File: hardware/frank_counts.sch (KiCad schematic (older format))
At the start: 1 part

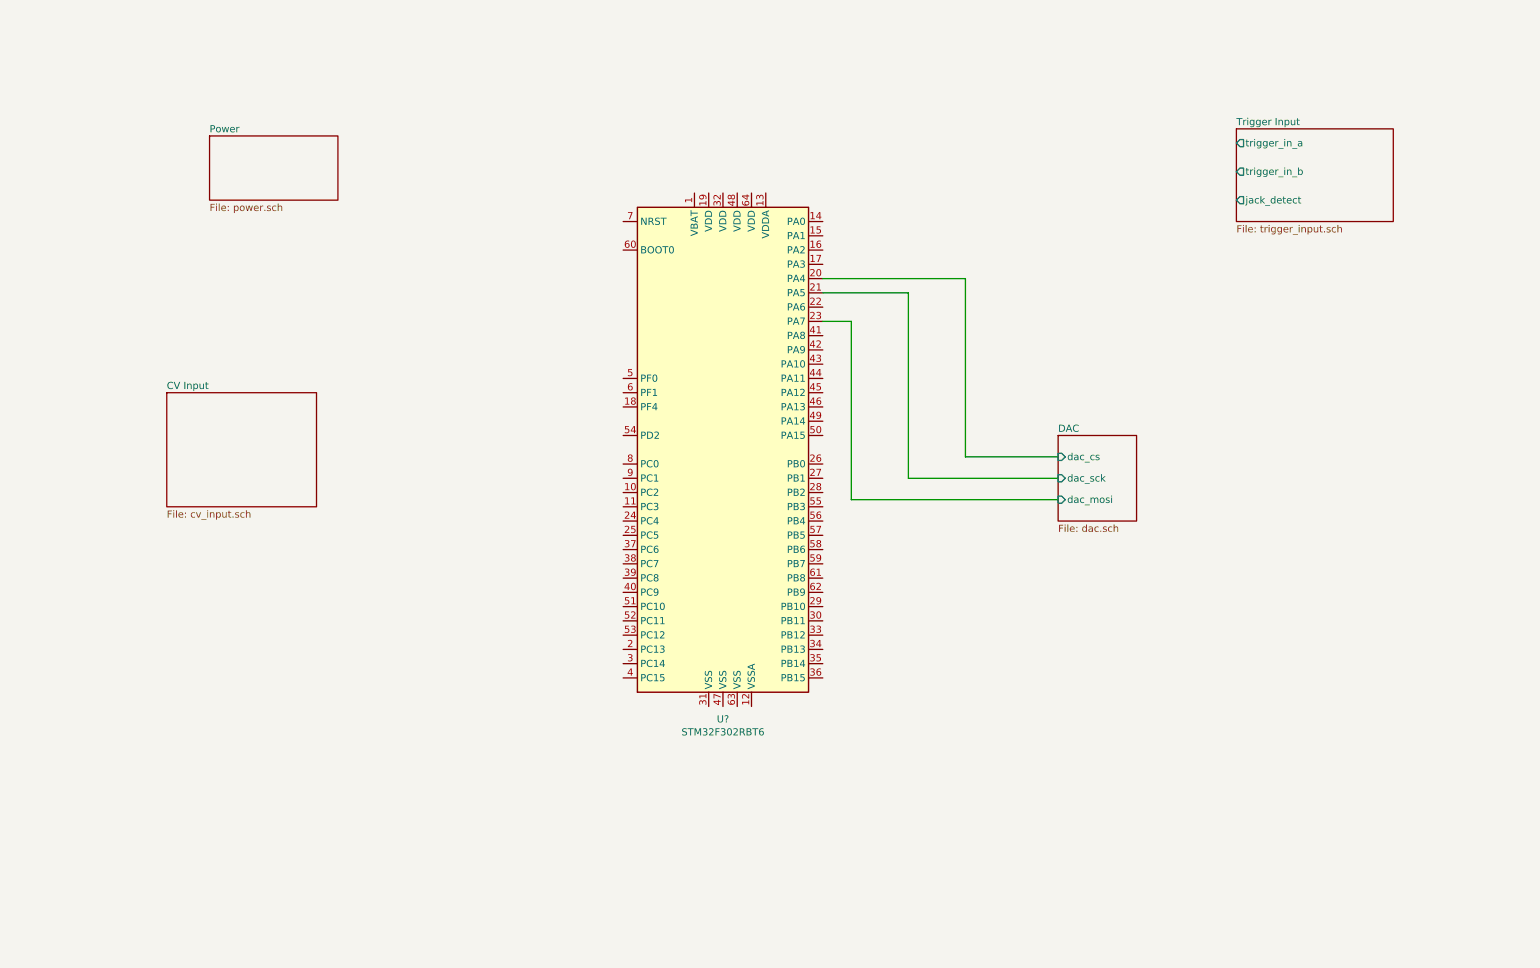
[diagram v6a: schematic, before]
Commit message: Add more schematics:
- Faders
- Step LEDs
- Trigger output
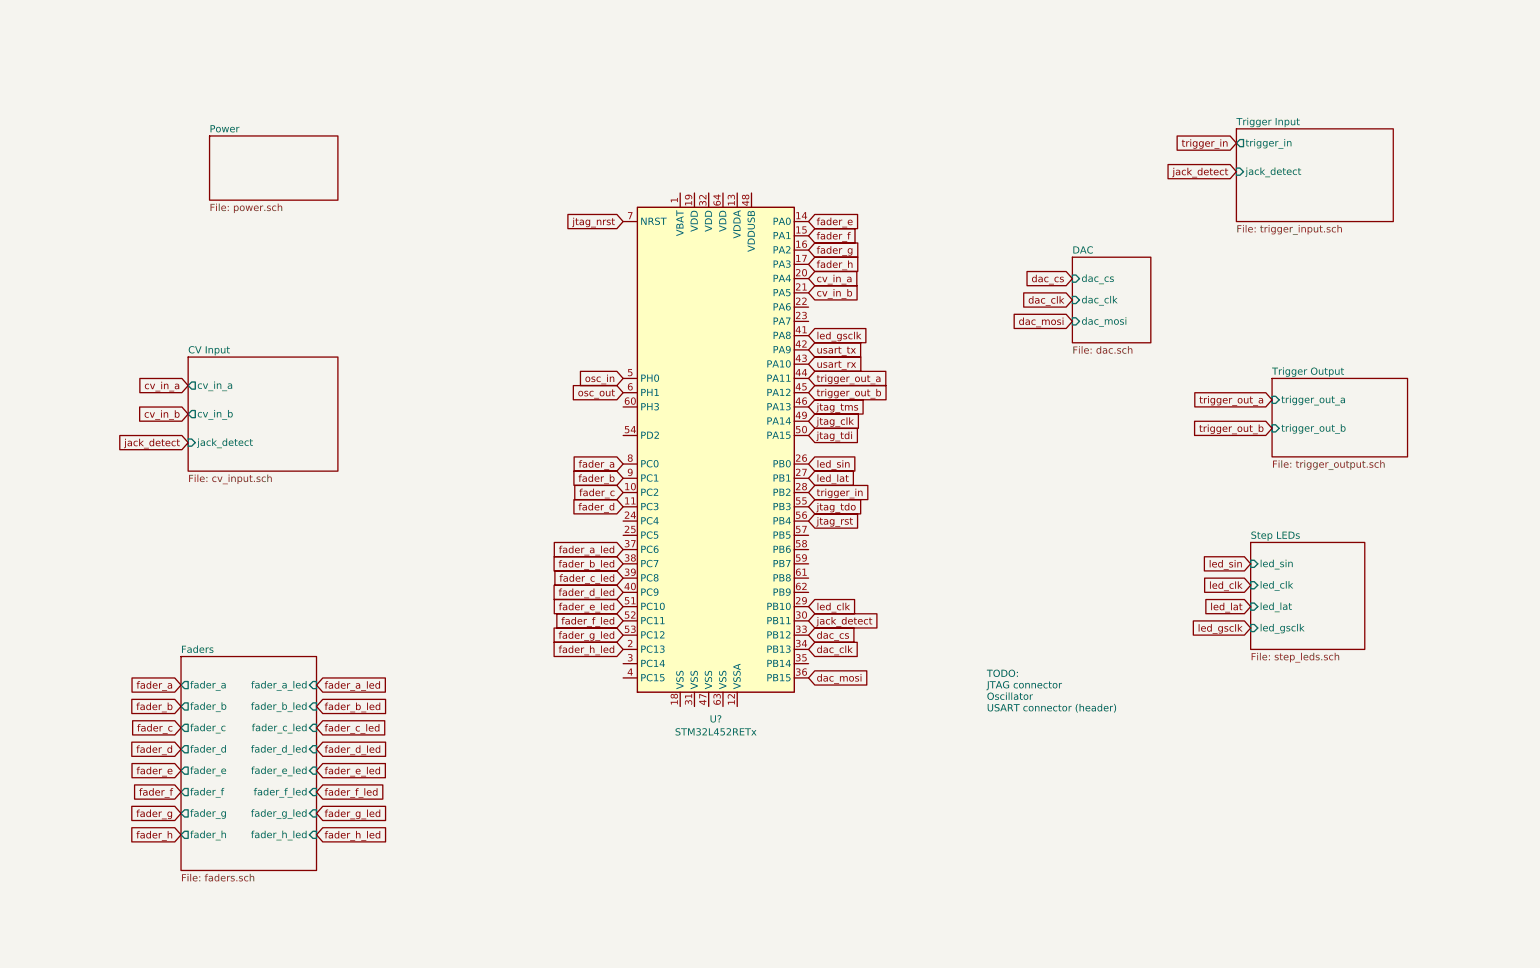
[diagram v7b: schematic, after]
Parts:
- removed U?: STM32F302RBT6, Package_QFP:LQFP-64_10x10mm_P0.5mm, symbol MCU_ST_STM32F3:STM32F302RBTx
- added U?: STM32L452RETx, Package_QFP:LQFP-64_10x10mm_P0.5mm, symbol MCU_ST_STM32L4:STM32L452RETx
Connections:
- new net cv_in_a: U?.20 (PA4)
- new net cv_in_b: U?.21 (PA5)
- new net dac_clk: U?.34 (PB13)
- new net dac_cs: U?.33 (PB12)
- new net dac_mosi: U?.36 (PB15)
- new net fader_a: U?.8 (PC0)
- new net fader_a_led: U?.37 (PC6)
- new net fader_b: U?.9 (PC1)
- new net fader_b_led: U?.38 (PC7)
- new net fader_c: U?.10 (PC2)
- new net fader_c_led: U?.39 (PC8)
- new net fader_d: U?.11 (PC3)
- new net fader_d_led: U?.40 (PC9)
- new net fader_e: U?.14 (PA0)
- new net fader_e_led: U?.51 (PC10)
- new net fader_f: U?.15 (PA1)
- new net fader_f_led: U?.52 (PC11)
- new net fader_g: U?.16 (PA2)
- new net fader_g_led: U?.53 (PC12)
- new net fader_h: U?.17 (PA3)
- new net fader_h_led: U?.2 (PC13)
- new net jack_detect: U?.30 (PB11)
- new net jtag_clk: U?.49 (PA14)
- new net jtag_nrst: U?.7 (NRST)
- new net jtag_rst: U?.56 (PB4)
- new net jtag_tdi: U?.50 (PA15)
- new net jtag_tdo: U?.55 (PB3)
- new net jtag_tms: U?.46 (PA13)
- new net led_clk: U?.29 (PB10)
- new net led_gsclk: U?.41 (PA8)
- new net led_lat: U?.27 (PB1)
- new net led_sin: U?.26 (PB0)
- new net osc_in: U?.5 (PH0)
- new net osc_out: U?.6 (PH1)
- new net trigger_in: U?.28 (PB2)
- new net trigger_out_a: U?.44 (PA11)
- new net trigger_out_b: U?.45 (PA12)
- new net usart_rx: U?.43 (PA10)
- new net usart_tx: U?.42 (PA9)
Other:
- note added: "TODO:\nJTAG connector\nOscillator\nUSART connector (header)"
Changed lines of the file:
@@
 $Descr A4 11693 8268
 encoding utf-8
-Sheet 1 6
+Sheet 1 9
 Title "frank.counts"
 Date "2020-05-04"
@@
 Comment4 ""
 $EndDescr
-Wire Wire Line
-	6150 2700 6350 2700
-Wire Wire Line
-	6150 2400 7150 2400
-Wire Wire Line
-	6150 2500 6750 2500
-Wire Wire Line
-	6350 2700 6350 3950
-Wire Wire Line
-	6350 3950 7800 3950
-Wire Wire Line
-	6750 2500 6750 3800
-Wire Wire Line
-	6750 3800 7800 3800
-Wire Wire Line
-	7150 2400 7150 3650
-Wire Wire Line
-	7150 3650 7800 3650
 $Sheet
 S 9050 1350 1100 650
@@
 F0 "Trigger Input" 50
 F1 "trigger_input.sch" 50
-F2 "jack_detect" O L 9050 1850 50
-F3 "trigger_in_a" O L 9050 1450 50
-F4 "trigger_in_b" O L 9050 1650 50
-$EndSheet
-$Sheet
-S 7800 3500 550  600
+F2 "trigger_in" O L 9050 1450 50
+F3 "jack_detect" I L 9050 1650 50
+$EndSheet
+$Sheet
+S 7900 2250 550  600
 U 5ED37B53
 F0 "DAC" 50
 F1 "dac.sch" 50
-F2 "dac_sck" I L 7800 3800 50
-F3 "dac_cs" I L 7800 3650 50
-F4 "dac_mosi" I L 7800 3950 50
-$EndSheet
-$Comp
-L MCU_ST_STM32F3:STM32F302RBTx U?
-U 1 1 5FBA4493
-P 5450 3600
-F 0 "U?" H 5450 1711 50  0000 C CNN
-F 1 "STM32F302RBT6" H 5450 1620 50  0000 C CNN
-F 2 "Package_QFP:LQFP-64_10x10mm_P0.5mm" H 4850 1900 50  0001 R CNN
-F 3 "http://www.st.com/st-web-ui/static/active/en/resource/technical/document/datasheet/DM00094064.pdf" H 5450 3600 50  0001 C CNN
-	1    5450 3600
-	1    0    0    -1
-$EndComp
-$Sheet
-S 1550 3200 1050 800
+F2 "dac_clk" I L 7900 2550 50
+F3 "dac_cs" I L 7900 2400 50
+F4 "dac_mosi" I L 7900 2700 50
+$EndSheet
+$Sheet
+S 1700 2950 1050 800
 U 5FCA3E21
 F0 "CV Input" 50
 F1 "cv_input.sch" 50
+F2 "cv_in_a" O L 1700 3150 50
+F3 "cv_in_b" O L 1700 3350 50
+F4 "jack_detect" I L 1700 3550 50
 $EndSheet
 $Sheet
@@
 F1 "power.sch" 50
 $EndSheet
+$Sheet
+S 1650 5050 950  1500
+U 5FD4CB96
+F0 "Faders" 50
+F1 "faders.sch" 50
+F2 "fader_a" O L 1650 5250 50
+F3 "fader_a_led" I R 2600 5250 50
+F4 "fader_b" O L 1650 5400 50
+F5 "fader_b_led" I R 2600 5400 50
+F6 "fader_c" O L 1650 5550 50
+F7 "fader_c_led" I R 2600 5550 50
+F8 "fader_d" O L 1650 5700 50
+F9 "fader_d_led" I R 2600 5700 50
+F10 "fader_e" O L 1650 5850 50
+F11 "fader_e_led" I R 2600 5850 50
+F12 "fader_f" O L 1650 6000 50
+F13 "fader_f_led" I R 2600 6000 50
+F14 "fader_g" O L 1650 6150 50
+F15 "fader_g_led" I R 2600 6150 50
+F16 "fader_h" O L 1650 6300 50
+F17 "fader_h_led" I R 2600 6300 50
+$EndSheet
+Text GLabel 1650 5250 0    50   Input ~ 0
+fader_a
+Text GLabel 4750 3700 0    50   Input ~ 0
+fader_a
+Text GLabel 1650 5400 0    50   Input ~ 0
+fader_b
+Text GLabel 1650 5550 0    50   Input ~ 0
+fader_c
+Text GLabel 1650 5700 0    50   Input ~ 0
+fader_d
+Text GLabel 1650 5850 0    50   Input ~ 0
+fader_e
+Text GLabel 1650 6000 0    50   Input ~ 0
+fader_f
+Text GLabel 1650 6150 0    50   Input ~ 0
+fader_g
+Text GLabel 1650 6300 0    50   Input ~ 0
+fader_h
+Text GLabel 4750 3800 0    50   Input ~ 0
+fader_b
+Text GLabel 4750 3900 0    50   Input ~ 0
+fader_c
+Text GLabel 4750 4000 0    50   Input ~ 0
+fader_d
+Text GLabel 6050 2000 2    50   Input ~ 0
+fader_e
+Text GLabel 6050 2100 2    50   Input ~ 0
+fader_f
+Text GLabel 6050 2200 2    50   Input ~ 0
+fader_g
+Text GLabel 6050 2300 2    50   Input ~ 0
+fader_h
+Text GLabel 2600 5250 2    50   Input ~ 0
+fader_a_led
+Text GLabel 2600 5400 2    50   Input ~ 0
+fader_b_led
+Text GLabel 2600 5550 2    50   Input ~ 0
+fader_c_led
+Text GLabel 2600 5700 2    50   Input ~ 0
+fader_d_led
+Text GLabel 2600 5850 2    50   Input ~ 0
+fader_e_led
+Text GLabel 2600 6000 2    50   Input ~ 0
+fader_f_led
+Text GLabel 2600 6150 2    50   Input ~ 0
+fader_g_led
+Text GLabel 2600 6300 2    50   Input ~ 0
+fader_h_led
+Text GLabel 4750 4300 0    50   Input ~ 0
+fader_a_led
+Text GLabel 4750 4400 0    50   Input ~ 0
+fader_b_led
+Text GLabel 4750 4500 0    50   Input ~ 0
+fader_c_led
+Text GLabel 4750 4600 0    50   Input ~ 0
+fader_d_led
+Text GLabel 4750 4700 0    50   Input ~ 0
+fader_e_led
+Text GLabel 4750 4800 0    50   Input ~ 0
+fader_f_led
+Text GLabel 4750 4900 0    50   Input ~ 0
+fader_g_led
+Text GLabel 4750 5000 0    50   Input ~ 0
+fader_h_led
+Text GLabel 7900 2400 0    50   Input ~ 0
+dac_cs
+Text GLabel 7900 2550 0    50   Input ~ 0
+dac_clk
+Text GLabel 7900 2700 0    50   Input ~ 0
+dac_mosi
+$Comp
+L MCU_ST_STM32L4:STM32L452RETx U?
+U 1 1 5FDEF22A
+P 5450 3600
+F 0 "U?" H 5400 1711 50  0000 C CNN
+F 1 "STM32L452RETx" H 5400 1620 50  0000 C CNN
+F 2 "Package_QFP:LQFP-64_10x10mm_P0.5mm" H 4850 1900 50  0001 R CNN
+F 3 "http://www.st.com/st-web-ui/static/active/en/resource/technical/document/datasheet/DM00340549.pdf" H 5450 3600 50  0001 C CNN
+	1    5450 3600
+	1    0    0    -1
+$EndComp
+Text GLabel 6050 4900 2    50   Input ~ 0
+dac_cs
+Text GLabel 6050 5000 2    50   Input ~ 0
+dac_clk
+Text GLabel 6050 5200 2    50   Input ~ 0
+dac_mosi
+$Sheet
+S 9150 4250 800  750
+U 5FDF6408
+F0 "Step LEDs" 50
+F1 "step_leds.sch" 50
+F2 "led_sin" I L 9150 4400 50
+F3 "led_clk" I L 9150 4550 50
+F4 "led_lat" I L 9150 4700 50
+F5 "led_gsclk" I L 9150 4850 50
+$EndSheet
+Text GLabel 6050 3700 2    50   Input ~ 0
+led_sin
+Text GLabel 9150 4400 0    50   Input ~ 0
+led_sin
+Text GLabel 6050 3800 2    50   Input ~ 0
+led_lat
+Text GLabel 9150 4700 0    50   Input ~ 0
+led_lat
+Text GLabel 6050 4700 2    50   Input ~ 0
+led_clk
+Text GLabel 9150 4550 0    50   Input ~ 0
+led_clk
+Text GLabel 6050 2800 2    50   Input ~ 0
+led_gsclk
+Text GLabel 9150 4850 0    50   Input ~ 0
+led_gsclk
+$Sheet
+S 9300 3100 950  550
+U 5FDBBE2F
+F0 "Trigger Output" 50
+F1 "trigger_output.sch" 50
+F2 "trigger_out_a" I L 9300 3250 50
+F3 "trigger_out_b" I L 9300 3450 50
+$EndSheet
+Text GLabel 6050 3300 2    50   Input ~ 0
+jtag_tms
+Text GLabel 6050 3400 2    50   Input ~ 0
+jtag_clk
+Text GLabel 6050 3500 2    50   Input ~ 0
+jtag_tdi
+Text GLabel 6050 4100 2    50   Input ~ 0
+jtag_rst
+Text GLabel 6050 4000 2    50   Input ~ 0
+jtag_tdo
+Text GLabel 4750 2000 0    50   Input ~ 0
+jtag_nrst
+Text GLabel 4750 3100 0    50   Input ~ 0
+osc_in
+Text GLabel 4750 3200 0    50   Input ~ 0
+osc_out
+Text GLabel 6050 2400 2    50   Input ~ 0
+cv_in_a
+Text GLabel 9300 3250 0    50   Input ~ 0
+trigger_out_a
+Text GLabel 9300 3450 0    50   Input ~ 0
+trigger_out_b
+Text GLabel 1700 3150 0    50   Input ~ 0
+cv_in_a
+Text GLabel 6050 2500 2    50   Input ~ 0
+cv_in_b
+Text GLabel 1700 3350 0    50   Input ~ 0
+cv_in_b
+Text Notes 7300 5450 0    50   ~ 0
+TODO:\nJTAG connector\nOscillator\nUSART connector (header)
+Text GLabel 9050 1450 0    50   Input ~ 0
+trigger_in
+Text GLabel 6050 2900 2    50   Input ~ 0
+usart_tx
+Text GLabel 6050 3000 2    50   Input ~ 0
+usart_rx
+Text GLabel 6050 3900 2    50   Input ~ 0
+trigger_in
+Text GLabel 6050 3100 2    50   Input ~ 0
+trigger_out_a
+Text GLabel 6050 3200 2    50   Input ~ 0
+trigger_out_b
+Text GLabel 6050 4800 2    50   Input ~ 0
+jack_detect
+Text GLabel 1700 3550 0    50   Input ~ 0
+jack_detect
+Text GLabel 9050 1650 0    50   Input ~ 0
+jack_detect
 $EndSCHEMATC

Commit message: Add encoder and pots
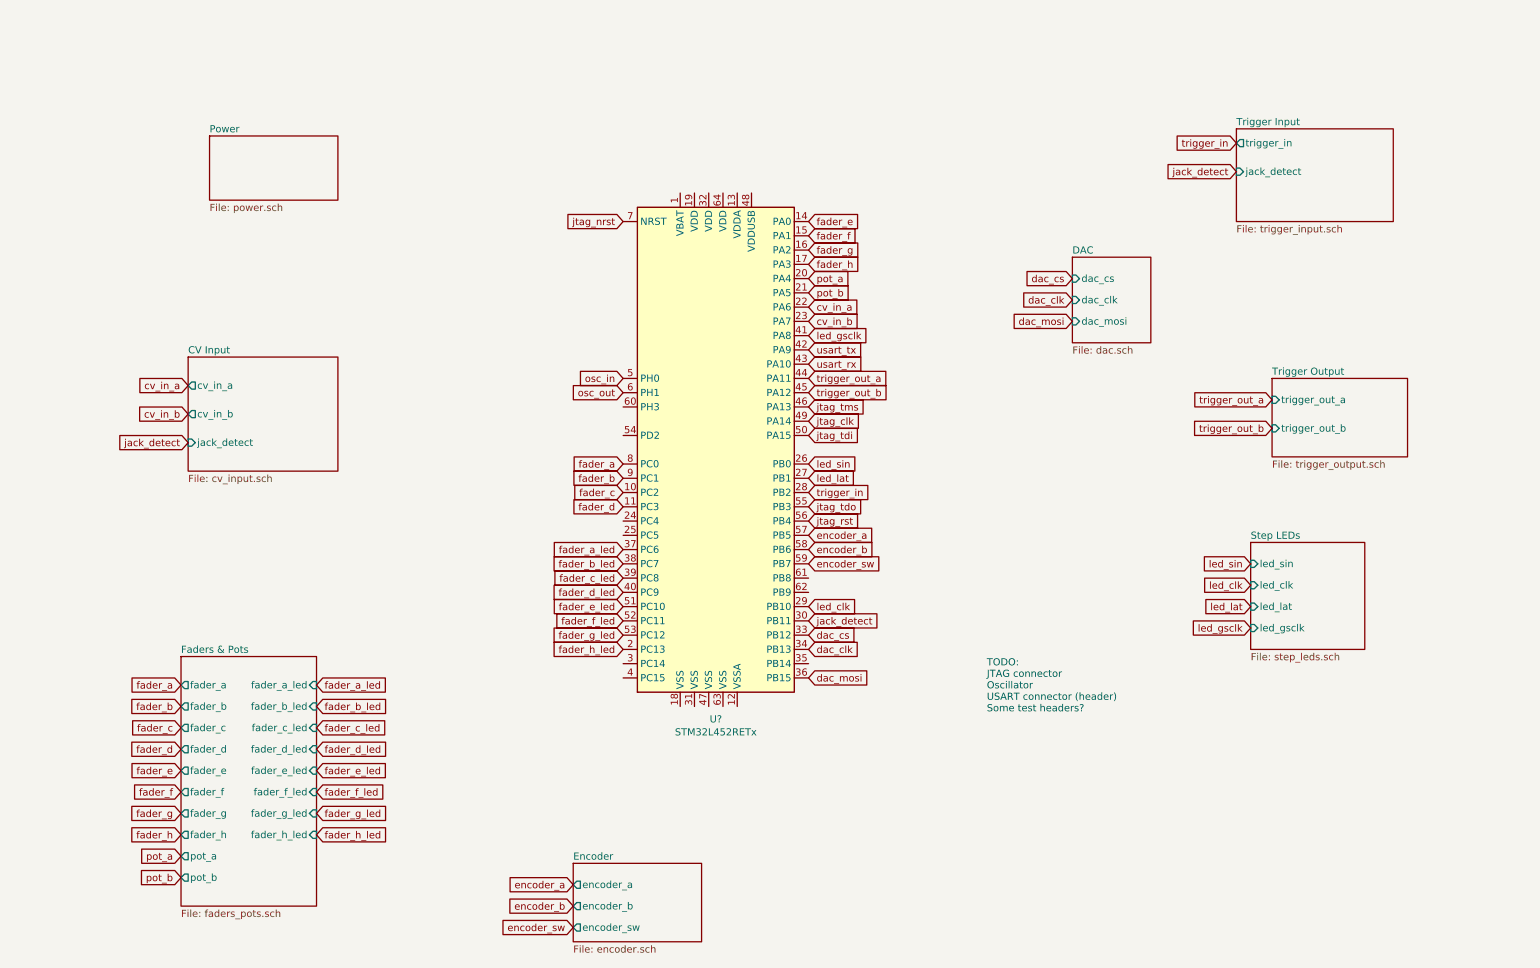
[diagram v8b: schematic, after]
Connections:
- net cv_in_a: now also U?.22 (PA6); no longer U?.20 (PA4)
- net cv_in_b: now also U?.23 (PA7); no longer U?.21 (PA5)
- net encoder_a: now reaches U?.57 (PB5)
- net encoder_b: now reaches U?.58 (PB6)
- net encoder_sw: now reaches U?.59 (PB7)
- new net pot_a: U?.20 (PA4)
- new net pot_b: U?.21 (PA5)
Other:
- note added: "TODO:\nJTAG connector\nOscillator\nUSART connector (header)\nSome test headers?"
- note removed: "TODO:\nJTAG connector\nOscillator\nUSART connector (header)"
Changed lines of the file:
@@
 $Descr A4 11693 8268
 encoding utf-8
-Sheet 1 9
+Sheet 1 10
 Title "frank.counts"
 Date "2020-05-04"
@@
 $EndSheet
 $Sheet
-S 1650 5050 950  1500
+S 1650 5050 950  1750
 U 5FD4CB96
-F0 "Faders" 50
-F1 "faders.sch" 50
+F0 "Faders & Pots" 50
+F1 "faders_pots.sch" 50
 F2 "fader_a" O L 1650 5250 50
 F3 "fader_a_led" I R 2600 5250 50
@@
 F16 "fader_h" O L 1650 6300 50
 F17 "fader_h_led" I R 2600 6300 50
+F18 "pot_a" O L 1650 6450 50
+F19 "pot_b" O L 1650 6600 50
 $EndSheet
 Text GLabel 1650 5250 0    50   Input ~ 0
@@
 Text GLabel 4750 3200 0    50   Input ~ 0
 osc_out
-Text GLabel 6050 2400 2    50   Input ~ 0
+Text GLabel 6050 2600 2    50   Input ~ 0
 cv_in_a
 Text GLabel 9300 3250 0    50   Input ~ 0
@@
 Text GLabel 1700 3150 0    50   Input ~ 0
 cv_in_a
-Text GLabel 6050 2500 2    50   Input ~ 0
+Text GLabel 6050 2700 2    50   Input ~ 0
 cv_in_b
 Text GLabel 1700 3350 0    50   Input ~ 0
 cv_in_b
 Text Notes 7300 5450 0    50   ~ 0
-TODO:\nJTAG connector\nOscillator\nUSART connector (header)
+TODO:\nJTAG connector\nOscillator\nUSART connector (header)\nSome test headers?
 Text GLabel 9050 1450 0    50   Input ~ 0
 trigger_in
@@
 Text GLabel 9050 1650 0    50   Input ~ 0
 jack_detect
+Text GLabel 6050 4200 2    50   Input ~ 0
+encoder_a
+Text GLabel 6050 4300 2    50   Input ~ 0
+encoder_b
+Text GLabel 6050 4400 2    50   Input ~ 0
+encoder_sw
+$Sheet
+S 4400 6500 900  550
+U 5FDF0A57
+F0 "Encoder" 50
+F1 "encoder.sch" 50
+F2 "encoder_b" O L 4400 6800 50
+F3 "encoder_a" O L 4400 6650 50
+F4 "encoder_sw" O L 4400 6950 50
+$EndSheet
+Text GLabel 4400 6650 0    50   Input ~ 0
+encoder_a
+Text GLabel 4400 6800 0    50   Input ~ 0
+encoder_b
+Text GLabel 4400 6950 0    50   Input ~ 0
+encoder_sw
+Text GLabel 6050 2400 2    50   Input ~ 0
+pot_a
+Text GLabel 6050 2500 2    50   Input ~ 0
+pot_b
+Text GLabel 1650 6450 0    50   Input ~ 0
+pot_a
+Text GLabel 1650 6600 0    50   Input ~ 0
+pot_b
 $EndSCHEMATC
